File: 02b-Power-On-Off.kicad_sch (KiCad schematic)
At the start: 11 parts, among them Q2 BSS138, Q3 DMG2305UX-7, Q4 DMG2305UX-7, SW5 SW_Push

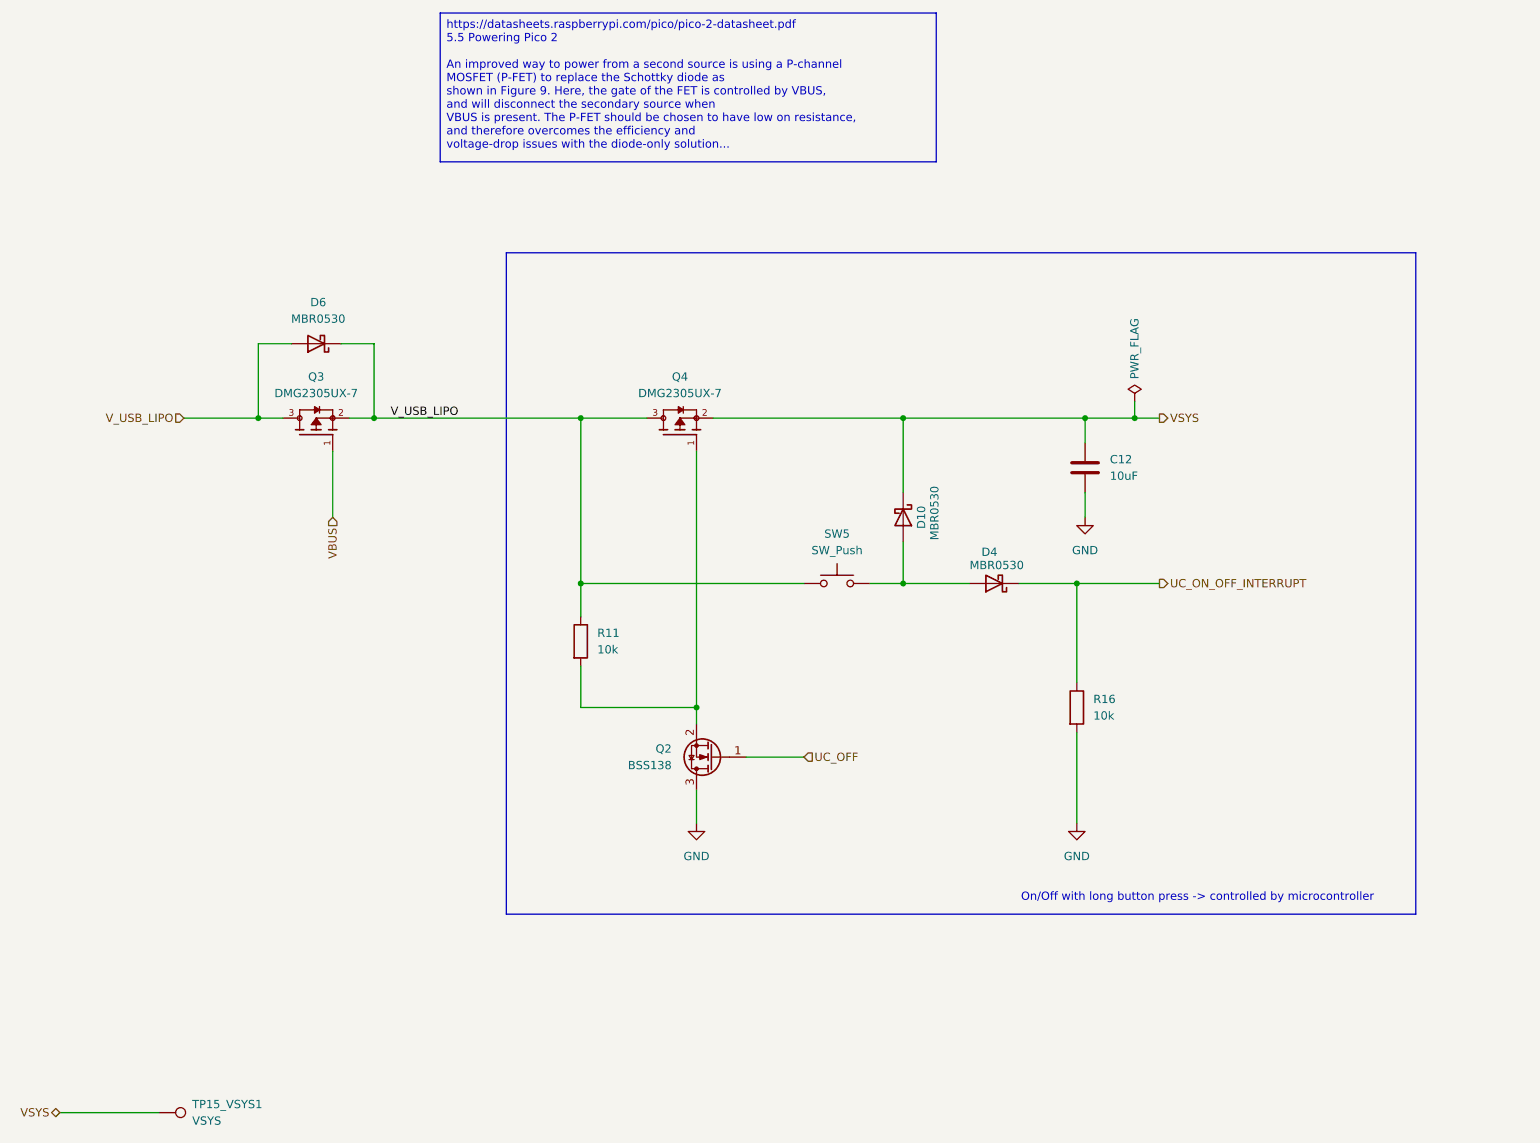
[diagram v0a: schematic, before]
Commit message: Worked on power on/off button, epaper driver and board/routing
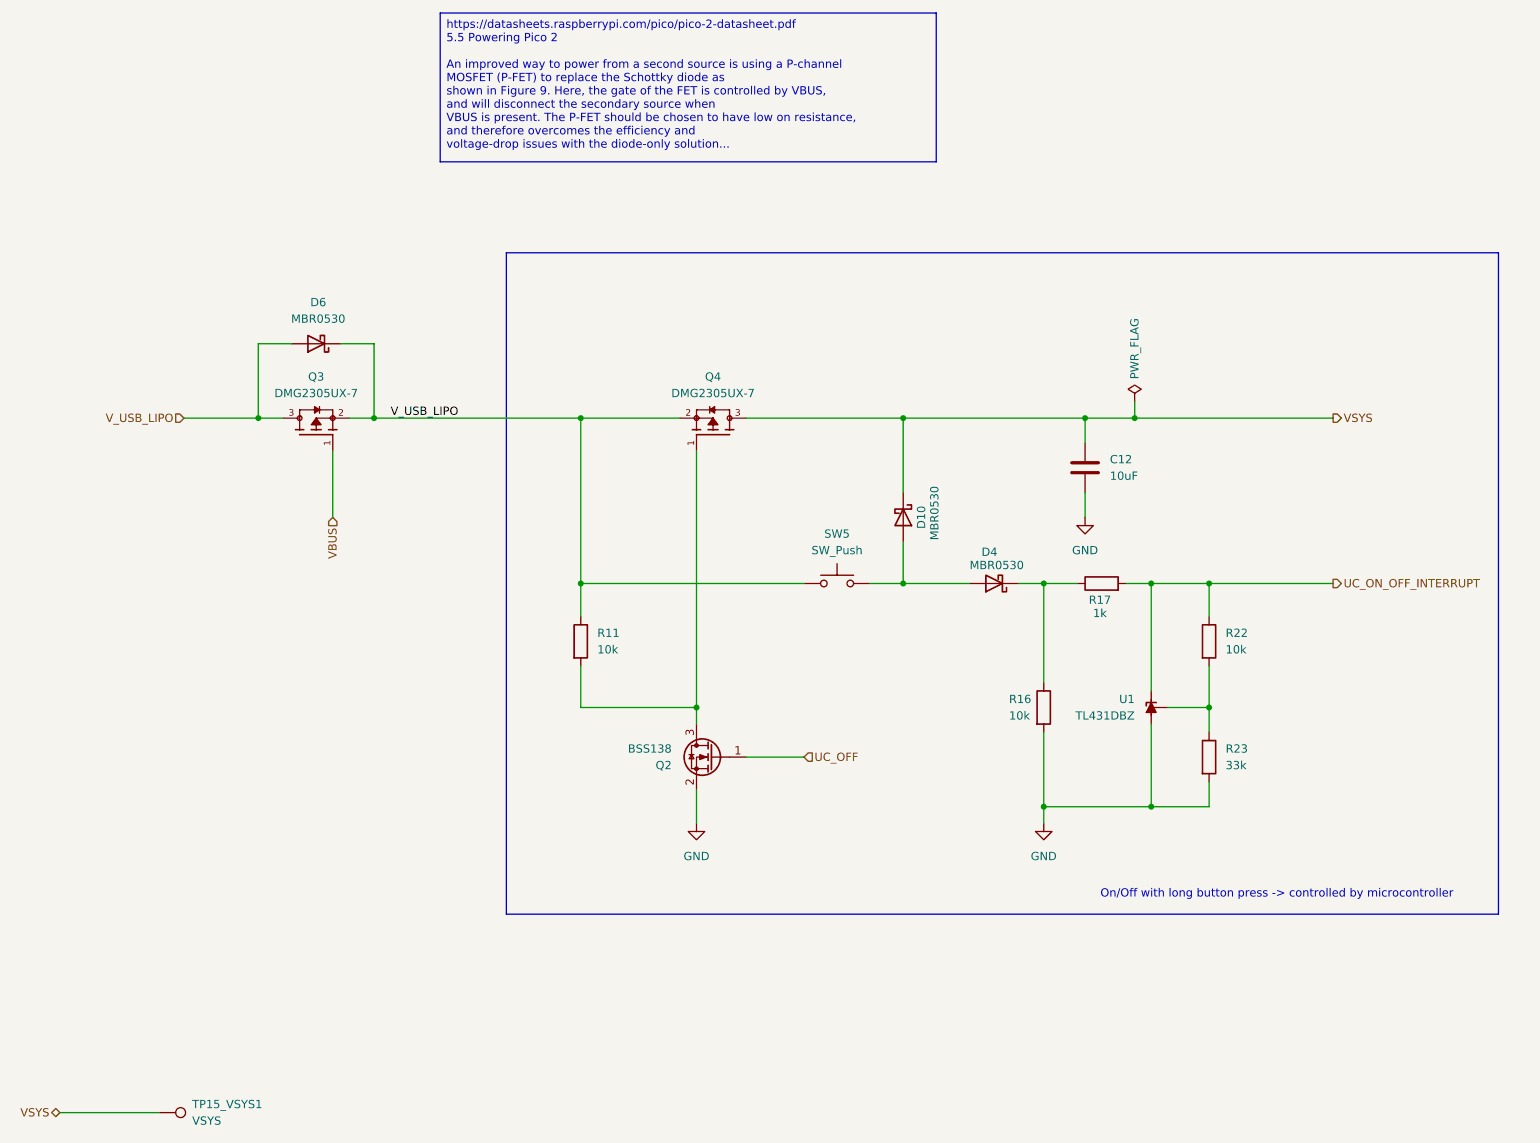
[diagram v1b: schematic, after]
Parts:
- added R17: 1k, Resistor_SMD:R_1206_3216Metric_Pad1.30x1.75mm_HandSolder, symbol Device:R
- added R22: 10k, Resistor_SMD:R_1206_3216Metric_Pad1.30x1.75mm_HandSolder, symbol Device:R
- added R23: 33k, Resistor_SMD:R_1206_3216Metric_Pad1.30x1.75mm_HandSolder, symbol Device:R
- added U1: TL431DBZ, Package_TO_SOT_SMD:SOT-23-3, symbol Reference_Voltage:TL431DBZ
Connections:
- net GND: now also Q2.2 (S), R23.2, U1.3 (A); no longer Q2.3 (D)
- net UC_ON_OFF_INTERRUPT: now also R17.2, R22.1, U1.1 (K); no longer D4.1 (K), R16.1
- net VSYS: now also Q4.3; no longer Q4.2
- net V_USB_LIPO: now also Q4.2; no longer Q4.3
- net at Q4.1, R11.2: now also Q2.3 (D); no longer Q2.2 (S)
- new net: D4.1 (K), R16.1, R17.1
- new net: R22.2, R23.1, U1.2 (REF)
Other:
- moved on the sheet: Q2, Q4, R16

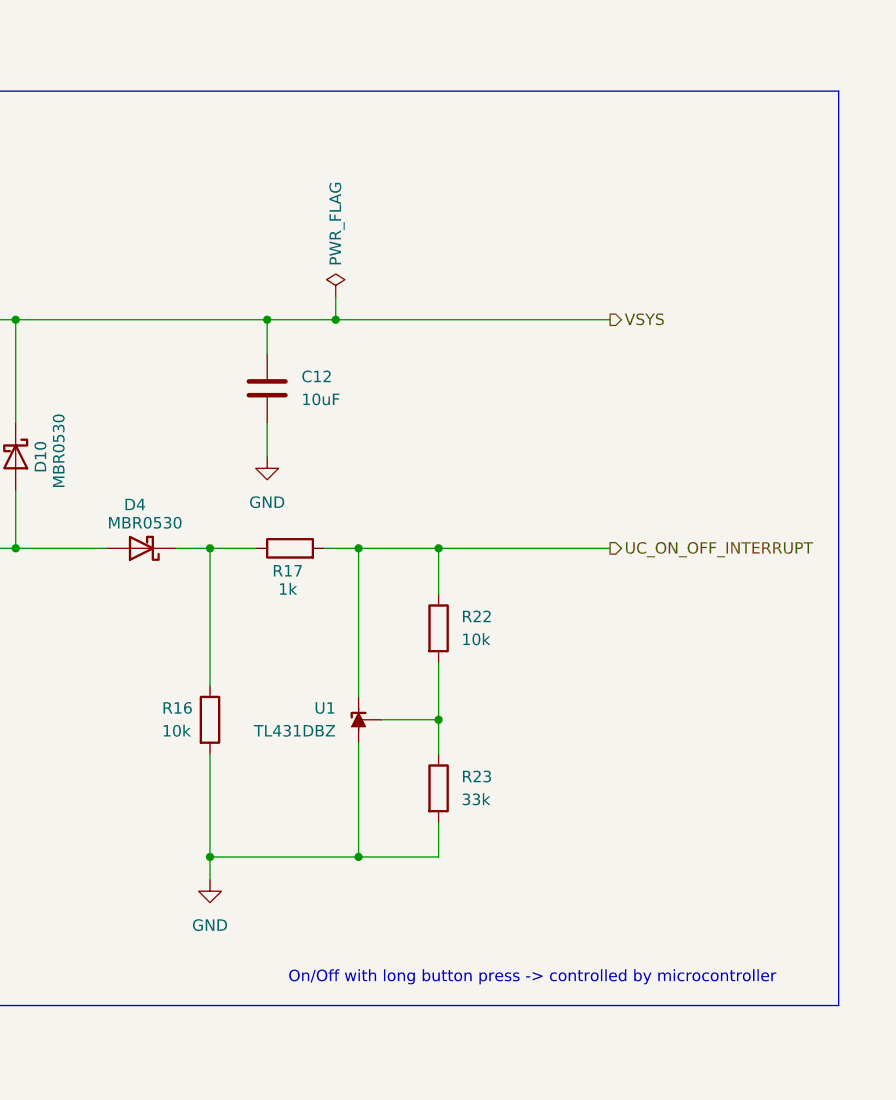
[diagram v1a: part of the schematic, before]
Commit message: v2: finished schematics, start routing
The schematics for v2 should be mostly finished by now.
The new on/off button is ready and tested with a breadboard setup.
It now uses two FETs for a self-holding circuit for turning the
device on and off. To reach a safe logic level for Pico 2, a
2.7V Zener diode is used together with a pull-down for E9 affected
RP2350 revisions.
Besides, most pull-up resistors are 10k now to keep the BoM
smaller.

Routing started with a major redesign.
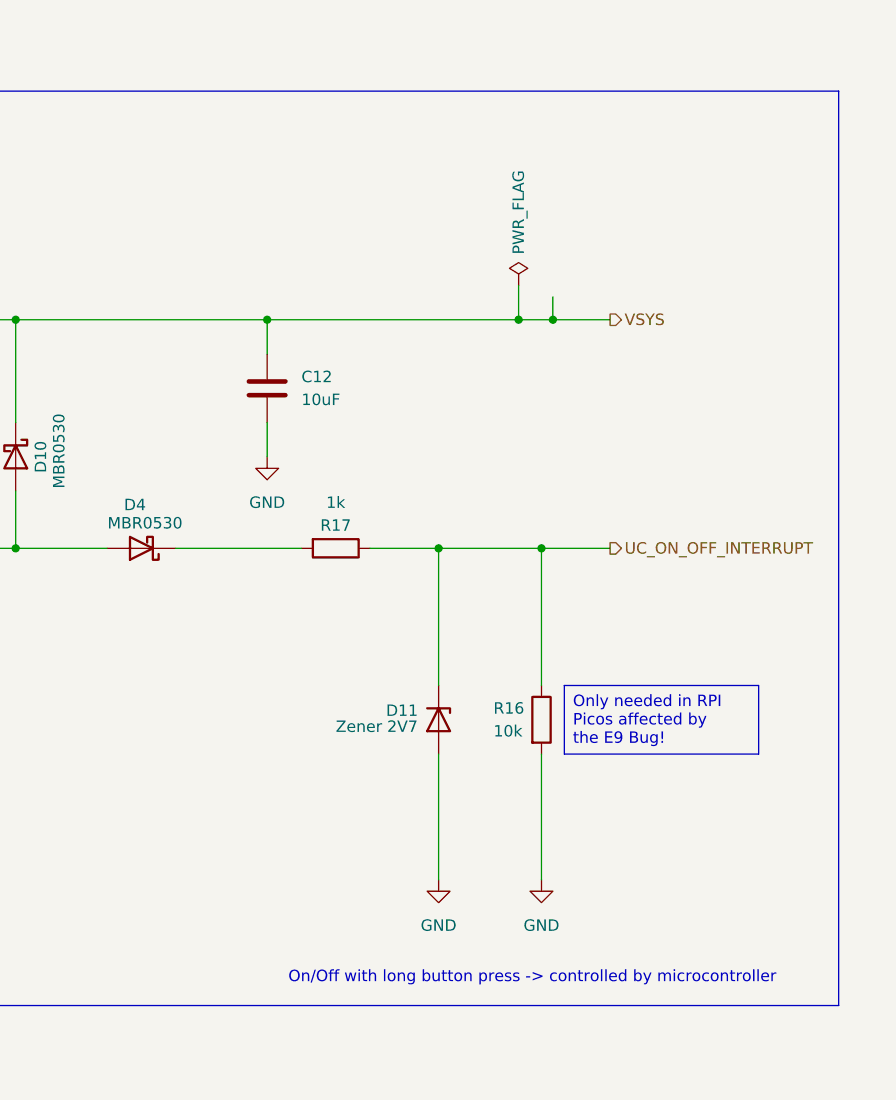
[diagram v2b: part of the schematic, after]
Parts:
- removed R22: 10k, Resistor_SMD:R_1206_3216Metric_Pad1.30x1.75mm_HandSolder, symbol Device:R
- removed R23: 33k, Resistor_SMD:R_1206_3216Metric_Pad1.30x1.75mm_HandSolder, symbol Device:R
- removed U1: TL431DBZ, Package_TO_SOT_SMD:SOT-23-3, symbol Reference_Voltage:TL431DBZ
- added D11: Zener 2V7, Diode_SMD:D_1206_3216Metric_Pad1.42x1.75mm_HandSolder, symbol Device:D_Zener
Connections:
- net GND: now also D11.2 (A)
- net UC_ON_OFF_INTERRUPT: now also R16.1, R17.1, D11.1 (K); no longer R17.2
- new net: D4.1 (K), R17.2
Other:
- moved on the sheet: R16

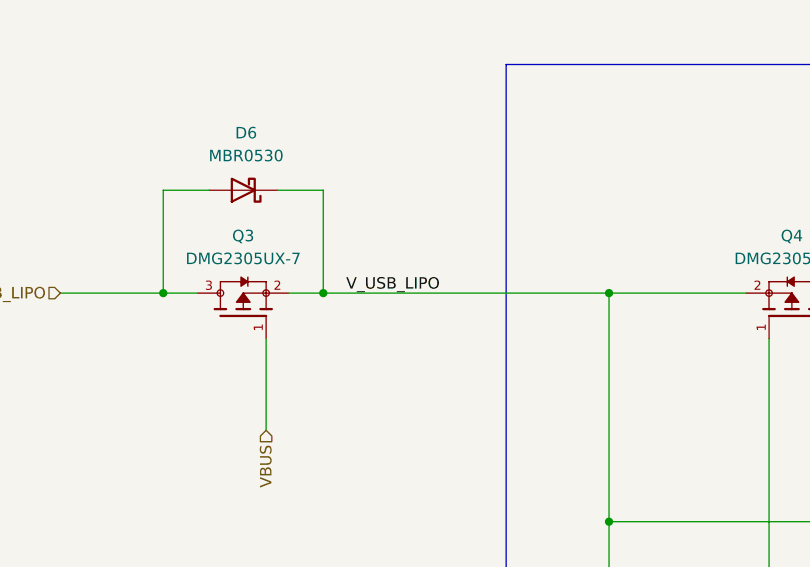
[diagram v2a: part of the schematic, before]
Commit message: First routing approach for v2
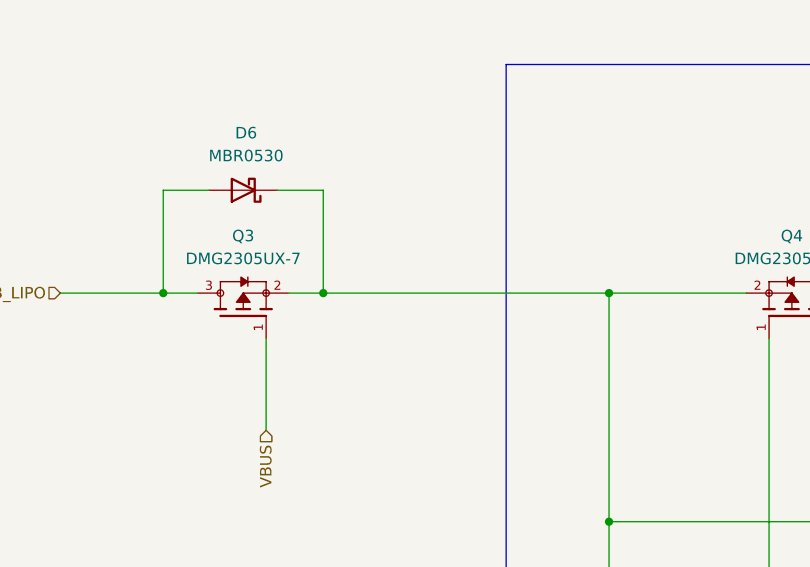
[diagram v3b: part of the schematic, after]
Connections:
- net V_USB_LIPO: no longer D6.1 (K), Q3.2, Q4.2, R11.1, SW5.1
- new net: D6.1 (K), Q3.2, Q4.2, R11.1, SW5.1
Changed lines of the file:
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@@
-		)
-	)
-	(label "V_USB_LIPO"
-		(at 83.82 76.2 0)
-		(effects
-			(font
-				(size 1.27 1.27)
-			)
-			(justify left bottom)
 		)
 	)
@@
 			(effects
 				(font
+					(size 1.27 1.27)
+					(italic yes)
+				)
+				(justify left)
+			)
+		)
+	)
+	(netclass_flag ""
+		(length 2.54)
+		(shape round)
+		(at 88.9 76.2 0)
+		(effects
+			(font
+				(size 1.27 1.27)
+			)
+			(justify left bottom)
+		)
+		(property "Netclass" "PWR"
+			(at 86.614 72.136 0)
+			(effects
+				(font
